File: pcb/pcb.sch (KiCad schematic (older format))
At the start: 30 parts, among them J1 BAT+, J10 GRN, J11 RED, J12 Load Cell, J2 BAT-, J3 Battery, J4 DS18B20, J5 TMP+, J6 TMPO, J7 TMP-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

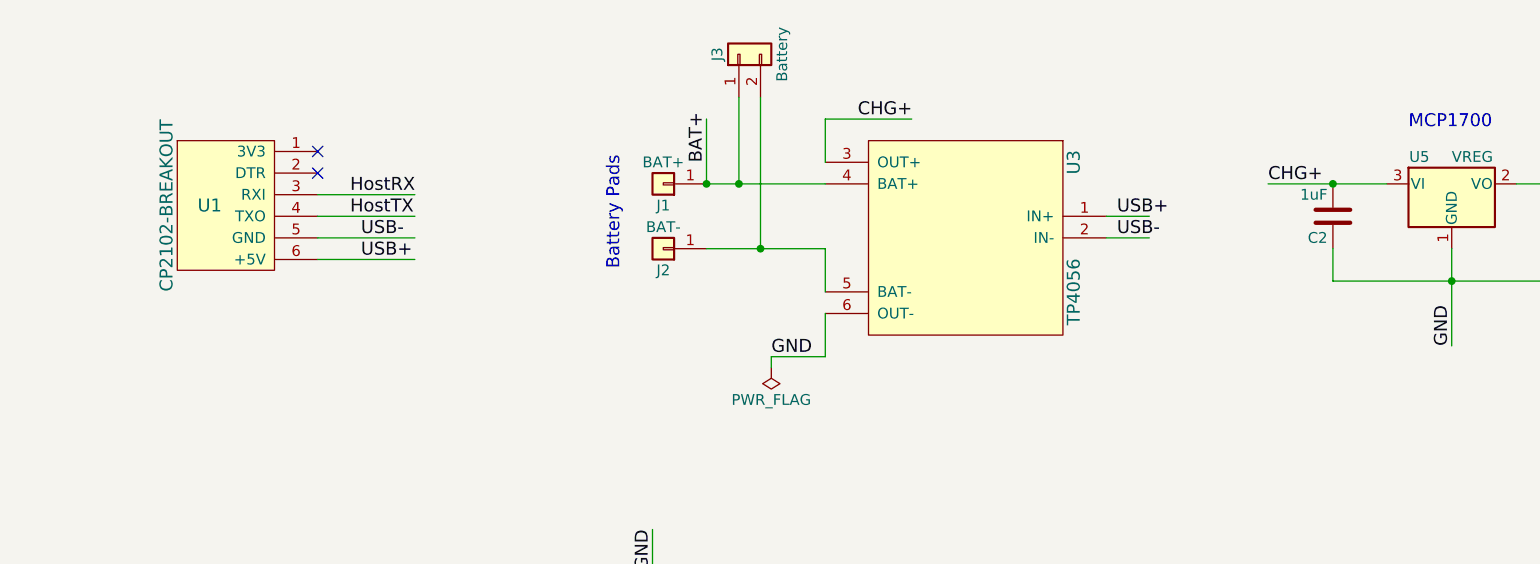
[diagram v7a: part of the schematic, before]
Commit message: Add capacitors across TP4056 OUT+/OUT-
I'm told this will fake a battery sufficiently well to keep from
confusing the TP4056 in the no-battery case. The two 47uF capacitors
can run the whole PCB in sleep mode for 2-3 seconds, and presumably
the non-sleep-mode load is sufficient to fool the TP4056.

I guess we'll see!
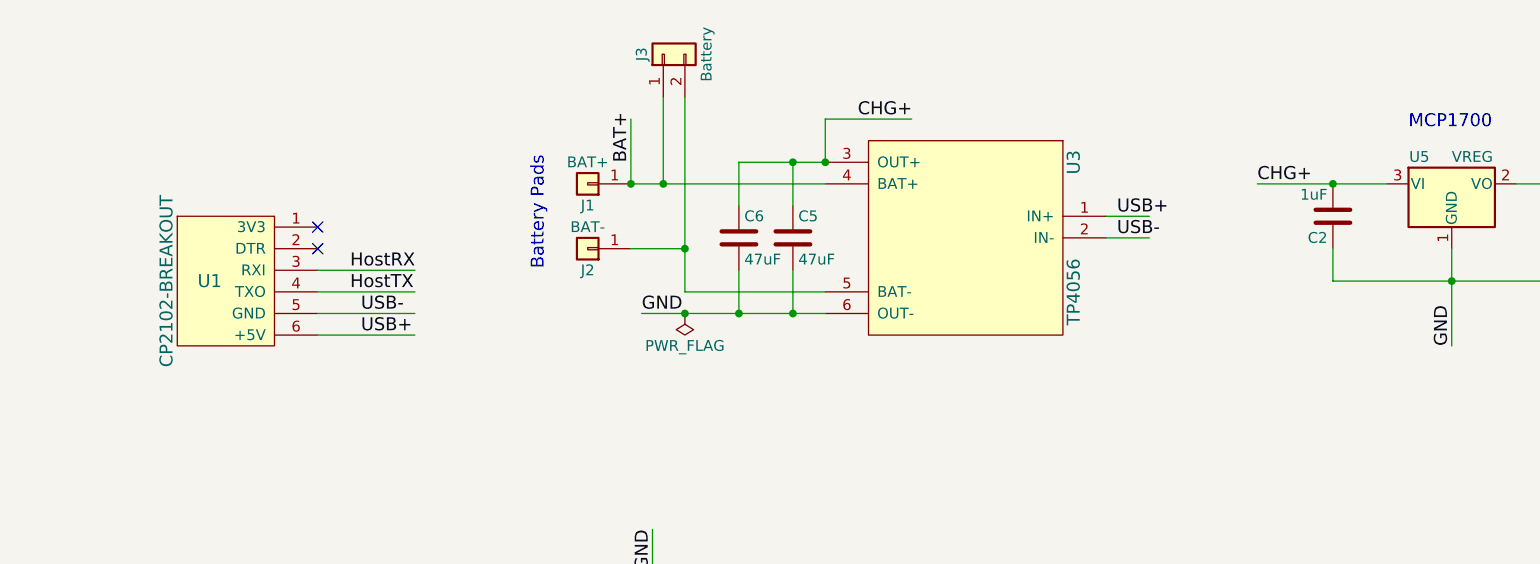
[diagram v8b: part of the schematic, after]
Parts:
- added C5, C6: 47uF, Capacitors_SMD:C_0805, symbol C
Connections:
- wire segments 84 -> 87
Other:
- moved on the sheet: J1, J2, J3, U1
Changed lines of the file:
@@
 L Conn_01x01 J1
 U 1 1 5B217852
-P 5200 2250
-F 0 "J1" H 5200 2350 50  0000 C CNN
-F 1 "BAT+" H 5200 2150 50  0000 C CNN
-F 2 "Extra_Pads:SolderWirePad_single_SMD_5x3mm" H 5200 2250 50  0001 C CNN
-F 3 "" H 5200 2250 50  0001 C CNN
-	1    5200 2250
+P 4850 2250
+F 0 "J1" H 4850 2350 50  0000 C CNN
+F 1 "BAT+" H 4850 2150 50  0000 C CNN
+F 2 "Extra_Pads:SolderWirePad_single_SMD_5x3mm" H 4850 2250 50  0001 C CNN
+F 3 "" H 4850 2250 50  0001 C CNN
+	1    4850 2250
 	-1   0    0    1
 $EndComp
@@
 L Conn_01x01 J2
 U 1 1 5B2178B3
-P 5200 2550
-F 0 "J2" H 5200 2650 50  0000 C CNN
-F 1 "BAT-" H 5200 2450 50  0000 C CNN
-F 2 "Extra_Pads:SolderWirePad_single_SMD_5x3mm" H 5200 2550 50  0001 C CNN
-F 3 "" H 5200 2550 50  0001 C CNN
-	1    5200 2550
+P 4850 2550
+F 0 "J2" H 4850 2650 50  0000 C CNN
+F 1 "BAT-" H 4850 2450 50  0000 C CNN
+F 2 "Extra_Pads:SolderWirePad_single_SMD_5x3mm" H 4850 2550 50  0001 C CNN
+F 3 "" H 4850 2550 50  0001 C CNN
+	1    4850 2550
 	-1   0    0    1
 $EndComp
@@
 	0    1    1    0
 $EndComp
-Text Label 3800 2600 0    60   ~ 0
+Text Label 3800 2950 0    60   ~ 0
 USB+
-Text Label 3750 2400 0    60   ~ 0
+Text Label 3750 2750 0    60   ~ 0
 HostTX
-Text Label 3750 2300 0    60   ~ 0
+Text Label 3750 2650 0    60   ~ 0
 HostRX
 Text Label 7300 2400 0    60   ~ 0
@@
 Text Label 7300 2500 0    60   ~ 0
 USB-
-Text Label 5700 3050 0    60   ~ 0
-GND
 Text Label 6100 1950 0    60   ~ 0
-CHG+
-Text Label 8000 2250 0    60   ~ 0
 CHG+
 Text Label 9850 2250 0    60   ~ 0
@@
 Text Label 8850 3000 1    60   ~ 0
 GND
-Text Label 5400 2150 1    60   ~ 0
+Text Label 5050 2150 1    60   ~ 0
 BAT+
-Text Label 3800 2500 0    60   ~ 0
+Text Label 3800 2850 0    60   ~ 0
 USB-
 Text Label 1950 4250 0    60   ~ 0
@@
 	1    0    0    -1
 $EndComp
-NoConn ~ 3600 2100
-NoConn ~ 3600 2200
-$Comp
-L PWR_FLAG #FLG01
-U 1 1 5B2225EE
-P 5700 3100
-F 0 "#FLG01" H 5700 3175 50  0001 C CNN
-F 1 "PWR_FLAG" H 5700 3250 50  0000 C CNN
-F 2 "" H 5700 3100 50  0001 C CNN
-F 3 "" H 5700 3100 50  0001 C CNN
-	1    5700 3100
-	-1   0    0    1
-$EndComp
-Text Notes 5100 2650 1    60   ~ 0
+NoConn ~ 3600 2450
+NoConn ~ 3600 2550
+Text Notes 4750 2650 1    60   ~ 0
 Battery Pads\n\n
 $Comp
 L Conn_01x02 J3
 U 1 1 5B22789F
-P 5550 1650
-F 0 "J3" H 5550 1750 50  0000 C CNN
-F 1 "Battery" H 5550 1450 50  0000 C CNN
-F 2 "Connectors_Molex:Molex_PicoBlade_53048-0210_02x1.25mm_Angled" H 5550 1650 50  0001 C CNN
-F 3 "" H 5550 1650 50  0001 C CNN
-	1    5550 1650
+P 5200 1650
+F 0 "J3" H 5200 1750 50  0000 C CNN
+F 1 "Battery" H 5200 1450 50  0000 C CNN
+F 2 "Connectors_Molex:Molex_PicoBlade_53048-0210_02x1.25mm_Angled" H 5200 1650 50  0001 C CNN
+F 3 "" H 5200 1650 50  0001 C CNN
+	1    5200 1650
 	0    -1   -1   0
 $EndComp
@@
 L CP2102-BREAKOUT U1
 U 1 1 5B258589
-P 2950 2050
-F 0 "U1" H 3100 1750 60  0000 C CNN
-F 1 "CP2102-BREAKOUT" V 2900 1750 60  0000 C CNN
-F 2 "CP2102-BRK:CP2102-BREAKOUT" H 2950 2050 60  0001 C CNN
-F 3 "" H 2950 2050 60  0001 C CNN
-	1    2950 2050
+P 2950 2400
+F 0 "U1" H 3100 2100 60  0000 C CNN
+F 1 "CP2102-BREAKOUT" V 2900 2100 60  0000 C CNN
+F 2 "CP2102-BRK:CP2102-BREAKOUT" H 2950 2400 60  0001 C CNN
+F 3 "" H 2950 2400 60  0001 C CNN
+	1    2950 2400
 	1    0    0    -1
 $EndComp
@@
 GND
 $Comp
-L PWR_FLAG #FLG02
+L PWR_FLAG #FLG01
 U 1 1 5B29A23A
 P 3200 5600
-F 0 "#FLG02" H 3200 5675 50  0001 C CNN
+F 0 "#FLG01" H 3200 5675 50  0001 C CNN
 F 1 "PWR_FLAG" V 3250 5450 50  0000 C CNN
 F 2 "" H 3200 5600 50  0001 C CNN
@@
 $EndComp
 $Comp
-L PWR_FLAG #FLG03
+L PWR_FLAG #FLG02
 U 1 1 5B22D046
 P 3200 5400
-F 0 "#FLG03" H 3200 5475 50  0001 C CNN
+F 0 "#FLG02" H 3200 5475 50  0001 C CNN
 F 1 "PWR_FLAG" V 3250 5250 50  0000 C CNN
 F 2 "" H 3200 5400 50  0001 C CNN
@@
 	7450 2500 7250 2500
 Wire Wire Line
-	5950 2850 5950 3050
-Wire Wire Line
-	5950 3050 5700 3050
-Wire Wire Line
 	5950 2150 5950 1950
 Wire Wire Line
 	5950 1950 6350 1950
 Wire Wire Line
-	8000 2250 8550 2250
-Wire Wire Line
 	8850 2550 8850 3000
 Wire Wire Line
 	9150 2250 10050 2250
 Wire Wire Line
-	5400 2250 5950 2250
+	5050 2250 5950 2250
 Wire Wire Line
 	5750 5000 6150 5000
@@
 	3650 5000 3950 5000
 Wire Wire Line
-	5400 2250 5400 1950
-Connection ~ 5400 2250
-Wire Wire Line
-	5400 2550 5950 2550
-Wire Wire Line
-	5950 2550 5950 2750
-Wire Wire Line
-	5700 3050 5700 3100
-Wire Wire Line
-	5550 1850 5550 2250
-Connection ~ 5550 2250
-Wire Wire Line
-	5650 1850 5650 2550
-Connection ~ 5650 2550
+	5050 2250 5050 1950
+Connection ~ 5050 2250
+Wire Wire Line
+	5050 2550 5300 2550
+Wire Wire Line
+	5200 1850 5200 2250
+Connection ~ 5200 2250
+Wire Wire Line
+	5300 1850 5300 2750
+Connection ~ 5300 2550
 Wire Wire Line
 	3850 5700 3850 6500
@@
 	8300 2700 9550 2700
 Connection ~ 9550 2250
-Connection ~ 8300 2250
 Wire Wire Line
 	8300 2550 8300 2700
@@
 Connection ~ 8850 2700
 Wire Wire Line
-	3600 2400 4050 2400
-Wire Wire Line
-	3600 2300 4050 2300
-Wire Wire Line
-	3600 2500 4050 2500
-Wire Wire Line
-	3600 2600 4050 2600
+	3600 2750 4050 2750
+Wire Wire Line
+	3600 2650 4050 2650
+Wire Wire Line
+	3600 2950 4050 2950
 Wire Wire Line
 	7650 5450 7300 5450
@@
 	1150 4250 2150 4250
 Connection ~ 1200 6400
+$Comp
+L PWR_FLAG #FLG03
+U 1 1 5B2F14F2
+P 5300 2850
+F 0 "#FLG03" H 5300 2925 50  0001 C CNN
+F 1 "PWR_FLAG" H 5300 3000 50  0000 C CNN
+F 2 "" H 5300 2850 50  0001 C CNN
+F 3 "" H 5300 2850 50  0001 C CNN
+	1    5300 2850
+	-1   0    0    1
+$EndComp
+Connection ~ 5300 2850
+Connection ~ 8300 2250
+Wire Wire Line
+	3600 2850 4050 2850
+Wire Wire Line
+	5100 2850 5950 2850
+$Comp
+L C C5
+U 1 1 5B301162
+P 5800 2500
+F 0 "C5" H 5825 2600 50  0000 L CNN
+F 1 "47uF" H 5825 2400 50  0000 L CNN
+F 2 "Capacitors_SMD:C_0805" H 5838 2350 50  0001 C CNN
+F 3 "" H 5800 2500 50  0001 C CNN
+	1    5800 2500
+	1    0    0    -1
+$EndComp
+Wire Wire Line
+	5300 2750 5950 2750
+Wire Wire Line
+	5550 2150 5950 2150
+Wire Wire Line
+	5800 2150 5800 2350
+Wire Wire Line
+	5800 2850 5800 2650
+Connection ~ 5800 2850
+Connection ~ 5950 2150
+Wire Wire Line
+	7950 2250 8550 2250
+Text Label 7950 2250 0    60   ~ 0
+CHG+
+Text Label 5100 2850 0    60   ~ 0
+GND
+$Comp
+L C C6
+U 1 1 5B3032B2
+P 5550 2500
+F 0 "C6" H 5575 2600 50  0000 L CNN
+F 1 "47uF" H 5575 2400 50  0000 L CNN
+F 2 "Capacitors_SMD:C_0805" H 5588 2350 50  0001 C CNN
+F 3 "" H 5550 2500 50  0001 C CNN
+	1    5550 2500
+	1    0    0    -1
+$EndComp
+Wire Wire Line
+	5550 2150 5550 2350
+Connection ~ 5800 2150
+Wire Wire Line
+	5550 2650 5550 2850
+Connection ~ 5550 2850
 $EndSCHEMATC
